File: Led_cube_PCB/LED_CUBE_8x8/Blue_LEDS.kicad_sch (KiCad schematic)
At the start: 100 parts, among them IC13 74AHCT244PW,118, IC14 74AHCT244PW,118, IC15 74AHCT244PW,118, IC17 74AHCT244PW,118, IC18 74AHCT244PW,118, IC23 74AHCT244PW,118, IC24 74AHCT244PW,118, IC25 74AHCT244PW,118, IC27 SN74HCS238DYYR, J7 Conn_02x16_Odd_Even, J8 Conn_02x16_Odd_Even

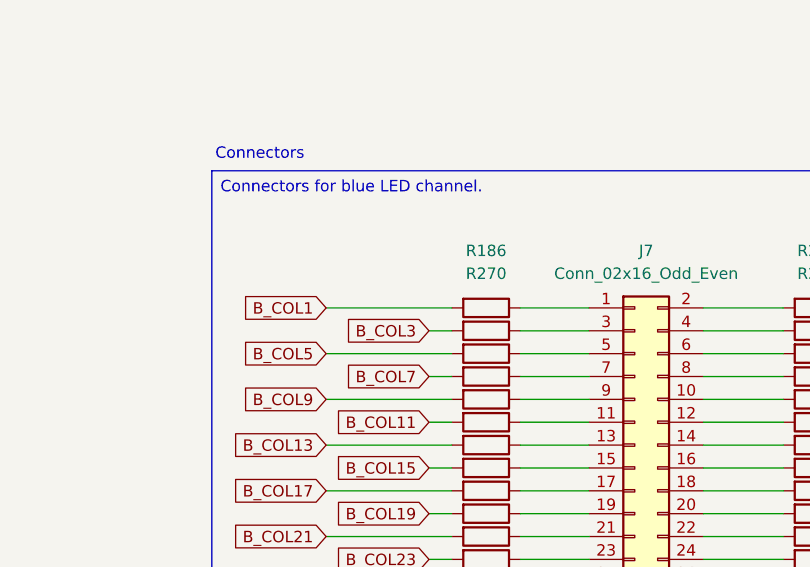
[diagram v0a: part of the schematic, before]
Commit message: Added test points and solder jumpers
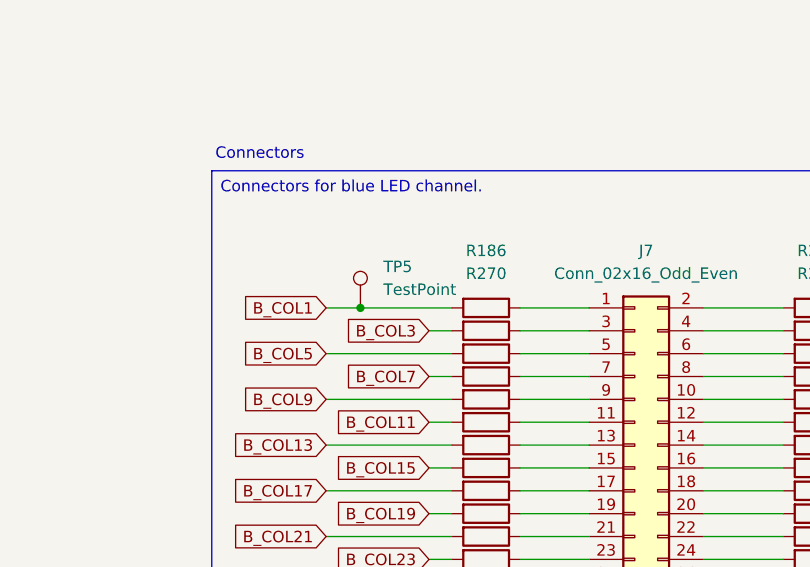
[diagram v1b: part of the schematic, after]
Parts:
- added TP5: TestPoint, TestPoint:TestPoint_Pad_D2.0mm, symbol Connector:TestPoint
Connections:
- net B_COL1: now also TP5.1
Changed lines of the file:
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@@
 	)
 	(junction
+		(at 303.53 100.33)
+		(diameter 0)
+		(color 0 0 0 0)
+	)
+	(junction
 		(at 204.47 38.1)
 		(diameter 0)
@@
 	(wire
 		(pts
-			(xy 299.72 100.33) (xy 313.69 100.33)
+			(xy 299.72 100.33) (xy 303.53 100.33)
 		)
 		(stroke
@@
 	(wire
 		(pts
+			(xy 303.53 100.33) (xy 313.69 100.33)
+		)
+		(stroke
+			(width 0)
+			(type default)
+		)
+	)
+	(wire
+		(pts
 			(xy 360.68 35.56) (xy 363.22 35.56)
 		)
@@
 			)
 		)
+	)
+	(symbol
+		(lib_id "Connector:TestPoint")
+		(at 303.53 100.33 0)
+		(unit 1)
+		(body_style 1)
+		(exclude_from_sim no)
+		(in_bom yes)
+		(on_board yes)
+		(in_pos_files yes)
+		(dnp no)
+		(fields_autoplaced yes)
+		(property "Reference" "TP5"
+			(at 306.07 95.7579 0)
+			(show_name no)
+			(do_not_autoplace no)
+			(effects
+				(font
+					(size 1.27 1.27)
+				)
+				(justify left)
+			)
+		)
+		(property "Value" "TestPoint"
+			(at 306.07 98.2979 0)
+			(show_name no)
+			(do_not_autoplace no)
+			(effects
+				(font
+					(size 1.27 1.27)
+				)
+				(justify left)
+			)
+		)
+		(property "Footprint" "TestPoint:TestPoint_Pad_D2.0mm"
+			(at 308.61 100.33 0)
+			(hide yes)
+			(show_name no)
+			(do_not_autoplace no)
+			(effects
+				(font
+					(size 1.27 1.27)
+				)
+			)
+		)
+		(property "Datasheet" ""
+			(at 308.61 100.33 0)
+			(hide yes)
+			(show_name no)
+			(do_not_autoplace no)
+			(effects
+				(font
+					(size 1.27 1.27)
+				)
+			)
+		)
+		(property "Description" "test point"
+			(at 303.53 100.33 0)
+			(hide yes)
+			(show_name no)
+			(do_not_autoplace no)
+			(effects
+				(font
+					(size 1.27 1.27)
+				)
+			)
+		)
+		(pin "1"
+		)
+		(instances
+			(project "LED_CUBE_8x8"
+				(path "/b239677e-e361-4439-8200-63fb41f7e03c/cc8bd84f-da41-4d1f-b6a9-e2091cdfadf0"
+					(reference "TP5")
+					(unit 1)
+				)
+			)
+		)
